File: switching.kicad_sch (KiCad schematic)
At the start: 12 parts, among them K1 SANYOU_SRD_Form_C, K2 SANYOU_SRD_Form_C, Q2 S8050_SMD, Q3 S8050_SMD

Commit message: Footprint assignment
Footprints yet to be assigned:
-U1: 74LVC125APW
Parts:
- D1, D2: footprint Diode_THT:D_DO-41_SOD81_P10.16mm_Horizontal -> Diode_SMD:D_SOD-123
- JP1, JP2, JP3, JP4: footprint (none) -> Jumper:SolderJumper-3_P2.0mm_Open_TrianglePad1.0x1.5mm
- Q2, Q3: footprint Diode_SMD:D_3220_8050Metric -> Package_TO_SOT_SMD:SOT-23
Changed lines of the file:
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@@
       (effects (font (size 1.27 1.27)) (justify left))
     )
-    (property "Footprint" "Diode_SMD:D_3220_8050Metric" (id 2) (at 208.28 120.015 0)
+    (property "Footprint" "Package_TO_SOT_SMD:SOT-23" (id 2) (at 208.28 120.015 0)
       (effects (font (size 1.27 1.27)) hide)
     )
@@
       (effects (font (size 1.27 1.27)) (justify left))
     )
-    (property "Footprint" "" (id 2) (at 87.63 107.315 0)
+    (property "Footprint" "Jumper:SolderJumper-3_P2.0mm_Open_TrianglePad1.0x1.5mm" (id 2) (at 87.63 107.315 0)
       (effects (font (size 1.27 1.27)) hide)
     )
@@
       (effects (font (size 1.27 1.27)) (justify left))
     )
-    (property "Footprint" "" (id 2) (at 110.49 80.645 0)
+    (property "Footprint" "Jumper:SolderJumper-3_P2.0mm_Open_TrianglePad1.0x1.5mm" (id 2) (at 110.49 80.645 0)
       (effects (font (size 1.27 1.27)) hide)
     )
@@
       (effects (font (size 1.27 1.27)) (justify left))
     )
-    (property "Footprint" "Diode_SMD:D_3220_8050Metric" (id 2) (at 207.645 83.185 0)
+    (property "Footprint" "Package_TO_SOT_SMD:SOT-23" (id 2) (at 207.645 83.185 0)
       (effects (font (size 1.27 1.27)) hide)
     )
@@
     (property "Reference" "D2" (id 0) (at 190.1825 122.3985 0))
     (property "Value" "1N5819" (id 1) (at 190.1825 125.1736 0))
-    (property "Footprint" "Diode_THT:D_DO-41_SOD81_P10.16mm_Horizontal" (id 2) (at 190.5 132.08 0)
+    (property "Footprint" "Diode_SMD:D_SOD-123" (id 2) (at 190.5 132.08 0)
       (effects (font (size 1.27 1.27)) hide)
     )
@@
     (property "Reference" "D1" (id 0) (at 190.1825 84.2985 0))
     (property "Value" "1N5819" (id 1) (at 190.1825 87.0736 0))
-    (property "Footprint" "Diode_THT:D_DO-41_SOD81_P10.16mm_Horizontal" (id 2) (at 190.5 93.98 0)
+    (property "Footprint" "Diode_SMD:D_SOD-123" (id 2) (at 190.5 93.98 0)
       (effects (font (size 1.27 1.27)) hide)
     )
@@
       (effects (font (size 1.27 1.27)) (justify left))
     )
-    (property "Footprint" "" (id 2) (at 110.49 107.315 0)
+    (property "Footprint" "Jumper:SolderJumper-3_P2.0mm_Open_TrianglePad1.0x1.5mm" (id 2) (at 110.49 107.315 0)
       (effects (font (size 1.27 1.27)) hide)
     )
@@
       (effects (font (size 1.27 1.27)) (justify left))
     )
-    (property "Footprint" "" (id 2) (at 87.63 80.645 0)
+    (property "Footprint" "Jumper:SolderJumper-3_P2.0mm_Open_TrianglePad1.0x1.5mm" (id 2) (at 87.63 80.645 0)
       (effects (font (size 1.27 1.27)) hide)
     )

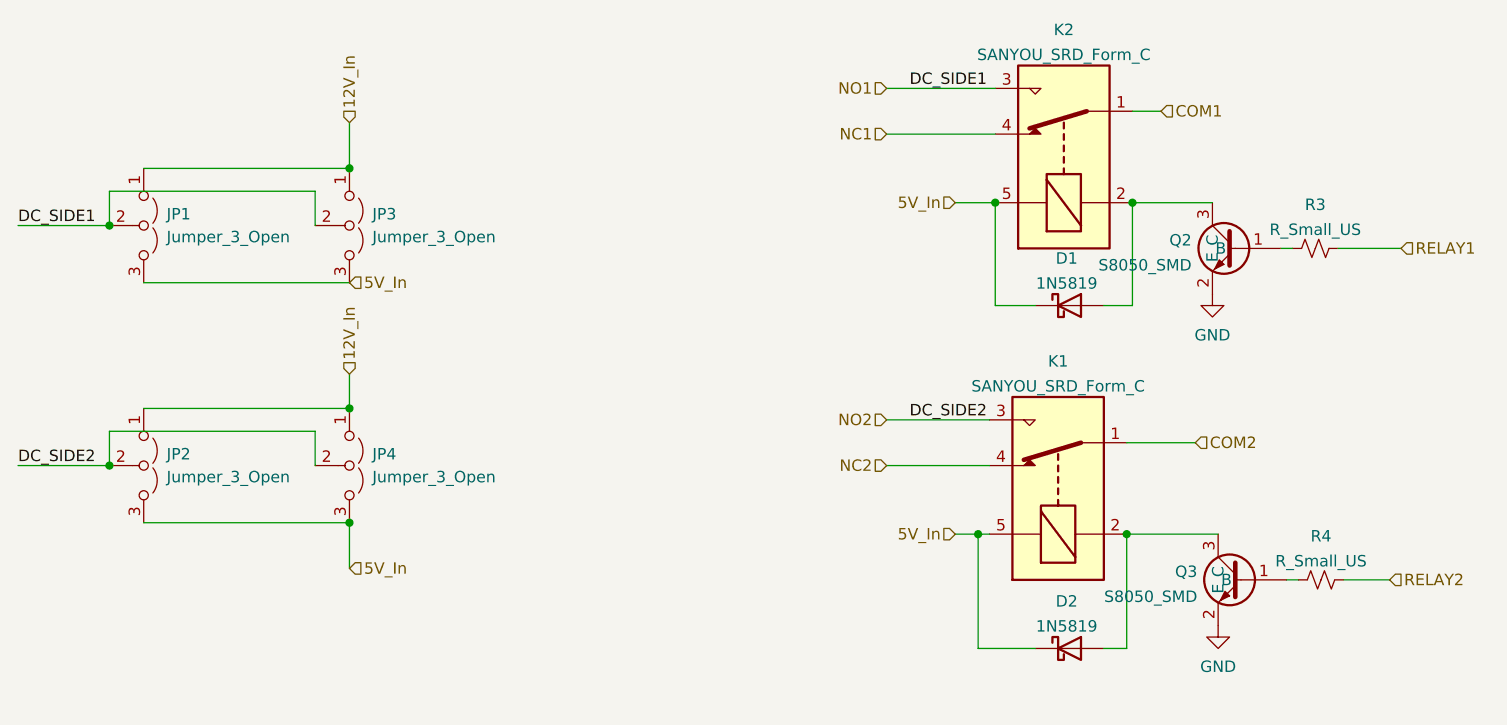
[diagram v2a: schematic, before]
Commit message: placement refinement and indicator LEDs for relays
-Crude wiring
-Fixed values
-Indicator LEDs for  relays
-Added test points
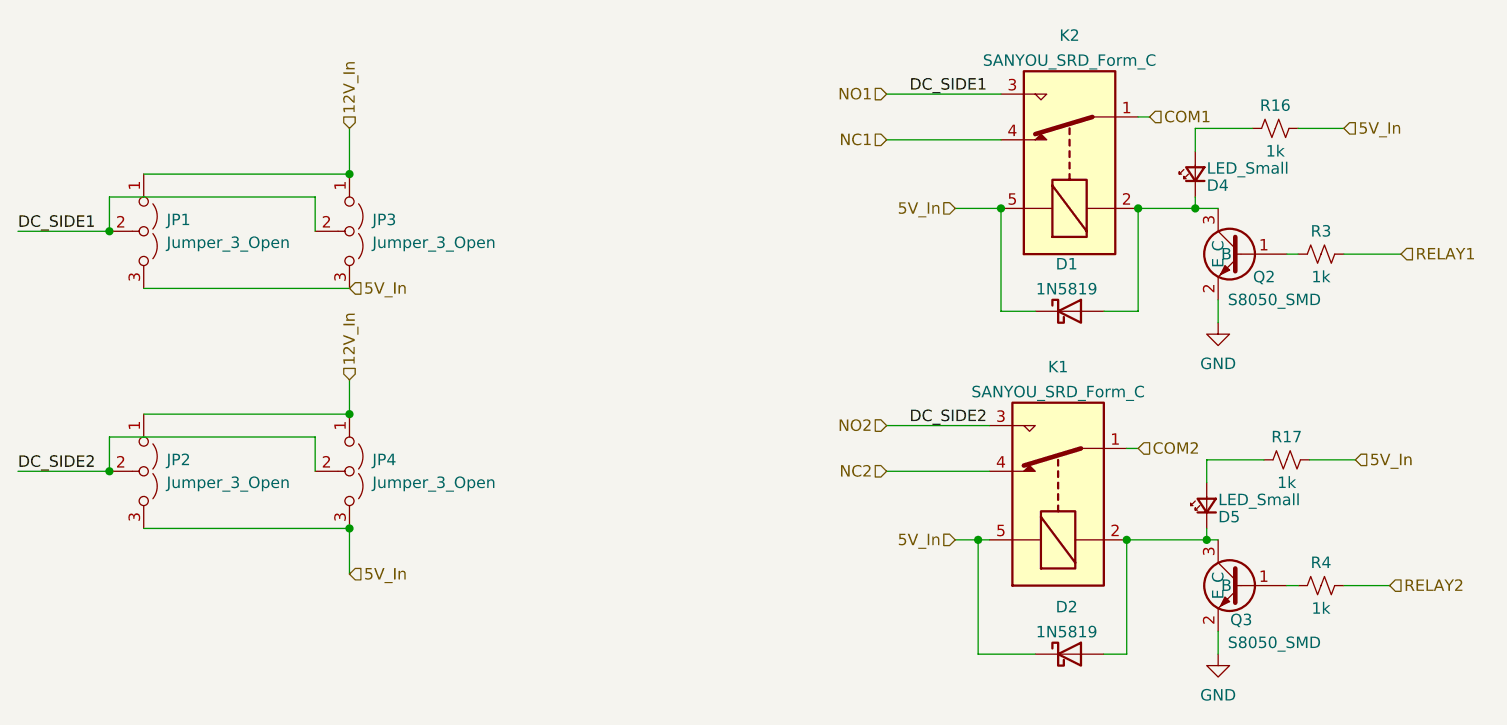
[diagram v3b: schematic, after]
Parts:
- added D4, D5: LED_Small, Diode_SMD:D_0603_1608Metric, symbol Device:LED_Small
- added R16, R17: 1k, Resistor_SMD:R_0402_1005Metric, symbol Device:R_Small_US
- R3, R4: value R_Small_US -> 1k
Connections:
- net 5V_In: now also R16.2, R17.2
- net at D1.2 (A), K2.2, Q2.3 (C): now also D4.1 (K)
- net at D2.2 (A), K1.2, Q3.3 (C): now also D5.1 (K)
- new net: D5.2 (A), R17.1
- new net: D4.2 (A), R16.1
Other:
- moved on the sheet: D1, D2, JP1, JP2, JP3, JP4, K1, K2, Q2, Q3, R3, R4

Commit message: Review and fixes on schematic and pcb.
-Updated Relay LED values.
-Fixed !RDY and R1 pin conflict on GPIO26.
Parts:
- D4, D5: value LED_Small -> Blue_LED
- R16, R17: value 1k -> 120R
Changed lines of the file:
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@@
       (effects (font (size 1.27 1.27)) (justify right))
     )
-    (property "Value" "LED_Small" (id 1) (at 207.01 111.125 90)
+    (property "Value" "Blue_LED" (id 1) (at 207.01 111.125 90)
       (effects (font (size 1.27 1.27)) (justify right))
     )
@@
     (in_bom yes) (on_board yes)
     (property "Reference" "R16" (id 0) (at 213.36 67.31 90))
-    (property "Value" "1k" (id 1) (at 213.36 72.39 90))
+    (property "Value" "120R" (id 1) (at 213.36 72.39 90))
     (property "Footprint" "Resistor_SMD:R_0402_1005Metric" (id 2) (at 213.36 69.85 0)
       (effects (font (size 1.27 1.27)) hide)
@@
       (effects (font (size 1.27 1.27)) (justify right))
     )
-    (property "Value" "LED_Small" (id 1) (at 205.74 74.295 90)
+    (property "Value" "Blue_LED" (id 1) (at 205.74 74.295 90)
       (effects (font (size 1.27 1.27)) (justify right))
     )
@@
     (in_bom yes) (on_board yes)
     (property "Reference" "R17" (id 0) (at 214.63 104.14 90))
-    (property "Value" "1k" (id 1) (at 214.63 109.22 90))
+    (property "Value" "120R" (id 1) (at 214.63 109.22 90))
     (property "Footprint" "Resistor_SMD:R_0402_1005Metric" (id 2) (at 214.63 106.68 0)
       (effects (font (size 1.27 1.27)) hide)

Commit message: Improvements made to the info in the schematic excel sheet and made the files necessary for production
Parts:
- D1, D2: Extended (none) -> 0; LCSC (none) -> C8598; Populate (none) -> 1; Price (none) -> 0.03
- D4, D5: Extended (none) -> 0; LCSC (none) -> C2286; Populate (none) -> 1; Price (none) -> 0.005
- JP1, JP2, JP3, JP4: Populate (none) -> 0
- K1, K2: Extended (none) -> 1; LCSC (none) -> C35449; Populate (none) -> 1
- Q2, Q3: Extended (none) -> 0; LCSC (none) -> C2150; Populate (none) -> 1
- R16, R17: Extended (none) -> 0; LCSC (none) -> C25079; Populate (none) -> 1
- R3, R4: Extended (none) -> 0; LCSC (none) -> C11702; Populate (none) -> 1
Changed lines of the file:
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@@
+      (effects (font (size 1.27 1.27)) hide)
+    )
+    (property "Populate" "1" (id 4) (at 190.5 73.66 0)
+      (effects (font (size 1.27 1.27)) hide)
+    )
+    (property "Extended" "1" (id 5) (at 190.5 73.66 0)
+      (effects (font (size 1.27 1.27)) hide)
+    )
+    (property "LCSC" "C35449" (id 6) (at 190.5 73.66 0)
       (effects (font (size 1.27 1.27)) hide)
     )
@@
       (effects (font (size 1.27 1.27)) hide)
     )
+    (property "Populate" "1" (id 4) (at 208.28 120.65 0)
+      (effects (font (size 1.27 1.27)) hide)
+    )
+    (property "Extended" "0" (id 5) (at 208.28 120.65 0)
+      (effects (font (size 1.27 1.27)) hide)
+    )
+    (property "LCSC" "C2150" (id 6) (at 208.28 120.65 0)
+      (effects (font (size 1.27 1.27)) hide)
+    )
     (pin "1")
     (pin "2")
@@
     )
     (property "Datasheet" "~" (id 3) (at 87.63 107.95 0)
+      (effects (font (size 1.27 1.27)) hide)
+    )
+    (property "Populate" "0" (id 4) (at 87.63 107.95 0)
       (effects (font (size 1.27 1.27)) hide)
     )
@@
     )
     (property "Datasheet" "~" (id 3) (at 205.74 111.76 90)
+      (effects (font (size 1.27 1.27)) hide)
+    )
+    (property "Extended" "0" (id 4) (at 205.74 111.76 0)
+      (effects (font (size 1.27 1.27)) hide)
+    )
+    (property "LCSC" "C2286" (id 5) (at 205.74 111.76 0)
+      (effects (font (size 1.27 1.27)) hide)
+    )
+    (property "Populate" "1" (id 6) (at 205.74 111.76 0)
+      (effects (font (size 1.27 1.27)) hide)
+    )
+    (property "Price" "0.005" (id 7) (at 205.74 111.76 0)
       (effects (font (size 1.27 1.27)) hide)
     )
@@
       (effects (font (size 1.27 1.27)) hide)
     )
+    (property "Populate" "1" (id 4) (at 213.36 69.85 0)
+      (effects (font (size 1.27 1.27)) hide)
+    )
+    (property "Extended" "0" (id 5) (at 213.36 69.85 0)
+      (effects (font (size 1.27 1.27)) hide)
+    )
+    (property "LCSC" "C25079" (id 6) (at 213.36 69.85 0)
+      (effects (font (size 1.27 1.27)) hide)
+    )
     (pin "1")
     (pin "2")
@@
       (effects (font (size 1.27 1.27)) hide)
     )
+    (property "Populate" "0" (id 4) (at 110.49 81.28 0)
+      (effects (font (size 1.27 1.27)) hide)
+    )
     (pin "1")
     (pin "2")
@@
     )
     (property "Datasheet" "" (id 3) (at 208.28 83.82 0)
+      (effects (font (size 1.27 1.27)) hide)
+    )
+    (property "Populate" "1" (id 4) (at 208.28 83.82 0)
+      (effects (font (size 1.27 1.27)) hide)
+    )
+    (property "Extended" "0" (id 5) (at 208.28 83.82 0)
+      (effects (font (size 1.27 1.27)) hide)
+    )
+    (property "LCSC" "C2150" (id 6) (at 208.28 83.82 0)
       (effects (font (size 1.27 1.27)) hide)
     )
@@
     )
     (property "Datasheet" "~" (id 3) (at 204.47 74.93 90)
+      (effects (font (size 1.27 1.27)) hide)
+    )
+    (property "Extended" "0" (id 4) (at 204.47 74.93 0)
+      (effects (font (size 1.27 1.27)) hide)
+    )
+    (property "LCSC" "C2286" (id 5) (at 204.47 74.93 0)
+      (effects (font (size 1.27 1.27)) hide)
+    )
+    (property "Populate" "1" (id 6) (at 204.47 74.93 0)
+      (effects (font (size 1.27 1.27)) hide)
+    )
+    (property "Price" "0.005" (id 7) (at 204.47 74.93 0)
       (effects (font (size 1.27 1.27)) hide)
     )
@@
       (effects (font (size 1.27 1.27)) hide)
     )
+    (property "Extended" "0" (id 4) (at 190.5 128.27 0)
+      (effects (font (size 1.27 1.27)) hide)
+    )
+    (property "LCSC" "C8598" (id 5) (at 190.5 128.27 0)
+      (effects (font (size 1.27 1.27)) hide)
+    )
+    (property "Populate" "1" (id 6) (at 190.5 128.27 0)
+      (effects (font (size 1.27 1.27)) hide)
+    )
+    (property "Price" "0.03" (id 7) (at 190.5 128.27 0)
+      (effects (font (size 1.27 1.27)) hide)
+    )
     (pin "1")
     (pin "2")
@@
       (effects (font (size 1.27 1.27)) hide)
     )
+    (property "Populate" "1" (id 4) (at 214.63 106.68 0)
+      (effects (font (size 1.27 1.27)) hide)
+    )
+    (property "Extended" "0" (id 5) (at 214.63 106.68 0)
+      (effects (font (size 1.27 1.27)) hide)
+    )
+    (property "LCSC" "C25079" (id 6) (at 214.63 106.68 0)
+      (effects (font (size 1.27 1.27)) hide)
+    )
     (pin "1")
     (pin "2")
@@
       (effects (font (size 1.27 1.27)) hide)
     )
+    (property "Extended" "0" (id 4) (at 190.5 90.17 0)
+      (effects (font (size 1.27 1.27)) hide)
+    )
+    (property "LCSC" "C8598" (id 5) (at 190.5 90.17 0)
+      (effects (font (size 1.27 1.27)) hide)
+    )
+    (property "Populate" "1" (id 6) (at 190.5 90.17 0)
+      (effects (font (size 1.27 1.27)) hide)
+    )
+    (property "Price" "0.03" (id 7) (at 190.5 90.17 0)
+      (effects (font (size 1.27 1.27)) hide)
+    )
     (pin "1")
     (pin "2")
@@
       (effects (font (size 1.27 1.27)) hide)
     )
+    (property "Populate" "1" (id 4) (at 218.44 120.65 0)
+      (effects (font (size 1.27 1.27)) hide)
+    )
+    (property "Extended" "0" (id 5) (at 218.44 120.65 0)
+      (effects (font (size 1.27 1.27)) hide)
+    )
+    (property "LCSC" "C11702" (id 6) (at 218.44 120.65 0)
+      (effects (font (size 1.27 1.27)) hide)
+    )
     (pin "1")
     (pin "2")
@@
     )
     (property "Datasheet" "~" (id 3) (at 110.49 107.95 0)
+      (effects (font (size 1.27 1.27)) hide)
+    )
+    (property "Populate" "0" (id 4) (at 110.49 107.95 0)
       (effects (font (size 1.27 1.27)) hide)
     )
@@
       (effects (font (size 1.27 1.27)) hide)
     )
+    (property "Populate" "1" (id 4) (at 189.23 110.49 0)
+      (effects (font (size 1.27 1.27)) hide)
+    )
+    (property "Extended" "1" (id 5) (at 189.23 110.49 0)
+      (effects (font (size 1.27 1.27)) hide)
+    )
+    (property "LCSC" "C35449" (id 6) (at 189.23 110.49 0)
+      (effects (font (size 1.27 1.27)) hide)
+    )
     (pin "1")
     (pin "2")
@@
       (effects (font (size 1.27 1.27)) hide)
     )
+    (property "Populate" "1" (id 4) (at 218.44 83.82 0)
+      (effects (font (size 1.27 1.27)) hide)
+    )
+    (property "Extended" "0" (id 5) (at 218.44 83.82 0)
+      (effects (font (size 1.27 1.27)) hide)
+    )
+    (property "LCSC" "C11702" (id 6) (at 218.44 83.82 0)
+      (effects (font (size 1.27 1.27)) hide)
+    )
     (pin "1")
     (pin "2")
@@
       (effects (font (size 1.27 1.27)) hide)
     )
+    (property "Populate" "0" (id 4) (at 87.63 81.28 0)
+      (effects (font (size 1.27 1.27)) hide)
+    )

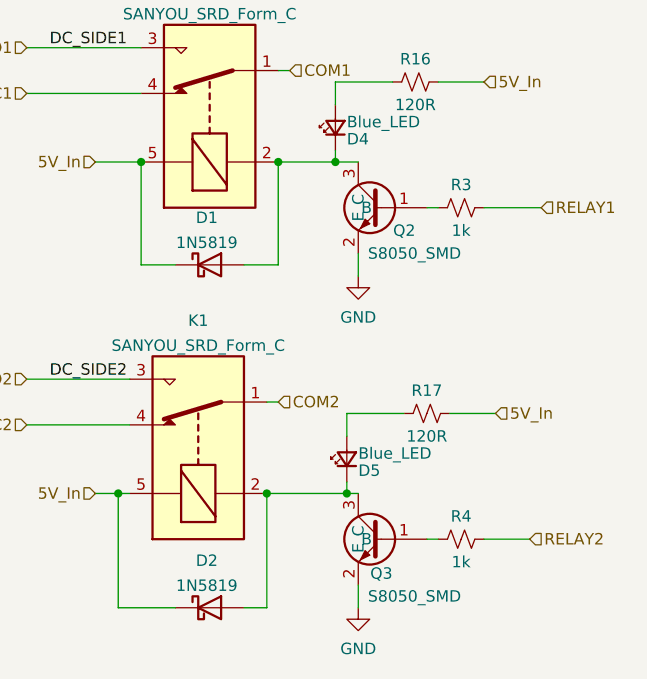
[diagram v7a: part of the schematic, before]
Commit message: Changes made to the AD7730 circuit. HX711 circuit added and AD7730 sidestepped.
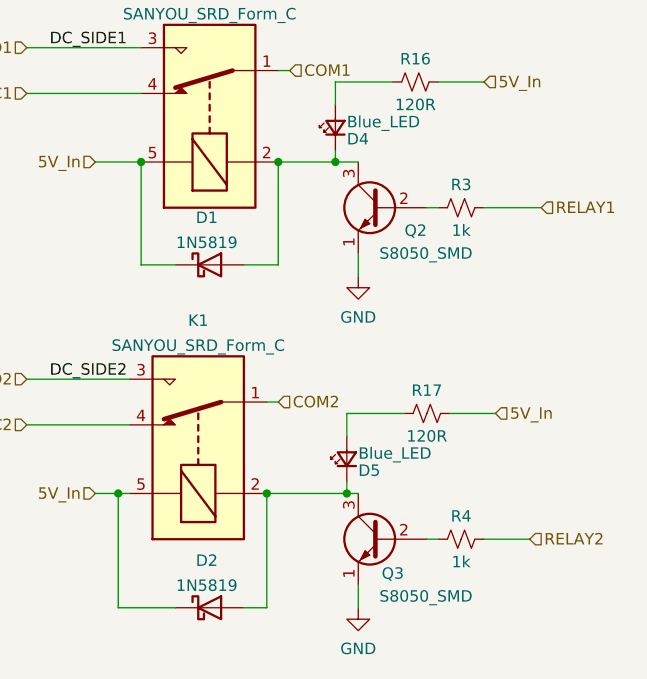
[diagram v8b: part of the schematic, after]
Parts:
- Q2, Q3: footprint Package_TO_SOT_SMD:SOT-23 -> Package_TO_SOT_THT:TO-92_Inline; symbol MyDevices:S8050_SMD -> Transistor_BJT:S8050
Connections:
- net GND: now also Q2.1 (E), Q3.1 (E); no longer Q2.2 (E), Q3.2 (E)
- net at R4.1: now also Q3.2 (B); no longer Q3.1 (B)
- net at R3.1: now also Q2.2 (B); no longer Q2.1 (B)
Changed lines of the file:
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@@
     )
   )
-  (symbol (lib_id "MyDevices:S8050_SMD") (at 208.28 120.65 0) (mirror y) (unit 1)
+  (symbol (lib_id "Transistor_BJT:S8050") (at 209.55 120.65 0) (mirror y) (unit 1)
     (in_bom yes) (on_board yes) (dnp no)
-    (property "Reference" "Q3" (at 210.82 124.46 0)
+    (property "Reference" "Q3" (at 212.09 124.46 0)
       (effects (font (size 1.27 1.27)) (justify left))
     )
-    (property "Value" "S8050_SMD" (at 218.44 127 0)
+    (property "Value" "S8050_SMD" (at 219.71 127 0)
       (effects (font (size 1.27 1.27)) (justify left))
     )
-    (property "Footprint" "Package_TO_SOT_SMD:SOT-23" (at 208.28 120.65 0)
+    (property "Footprint" "Package_TO_SOT_THT:TO-92_Inline" (at 204.47 122.555 0)
+      (effects (font (size 1.27 1.27) italic) (justify left) hide)
+    )
+    (property "Datasheet" "http://www.unisonic.com.tw/datasheet/S8050.pdf" (at 209.55 120.65 0)
+      (effects (font (size 1.27 1.27)) (justify left) hide)
+    )
+    (property "Populate" "1" (at 209.55 120.65 0)
       (effects (font (size 1.27 1.27)) hide)
     )
-    (property "Datasheet" "" (at 208.28 120.65 0)
+    (property "Extended" "0" (at 209.55 120.65 0)
       (effects (font (size 1.27 1.27)) hide)
     )
-    (property "Populate" "1" (at 208.28 120.65 0)
-      (effects (font (size 1.27 1.27)) hide)
-    )
-    (property "Extended" "0" (at 208.28 120.65 0)
-      (effects (font (size 1.27 1.27)) hide)
-    )
-    (property "LCSC" "C2150" (at 208.28 120.65 0)
+    (property "LCSC" "C2150" (at 209.55 120.65 0)
       (effects (font (size 1.27 1.27)) hide)
     )
@@
     )
   )
-  (symbol (lib_id "MyDevices:S8050_SMD") (at 208.28 83.82 0) (mirror y) (unit 1)
+  (symbol (lib_id "Transistor_BJT:S8050") (at 209.55 83.82 0) (mirror y) (unit 1)
     (in_bom yes) (on_board yes) (dnp no)
-    (property "Reference" "Q2" (at 213.36 86.36 0)
+    (property "Reference" "Q2" (at 214.63 86.36 0)
       (effects (font (size 1.27 1.27)) (justify left))
     )
-    (property "Value" "S8050_SMD" (at 218.44 88.9 0)
+    (property "Value" "S8050_SMD" (at 219.71 88.9 0)
       (effects (font (size 1.27 1.27)) (justify left))
     )
-    (property "Footprint" "Package_TO_SOT_SMD:SOT-23" (at 208.28 83.82 0)
+    (property "Footprint" "Package_TO_SOT_THT:TO-92_Inline" (at 204.47 85.725 0)
+      (effects (font (size 1.27 1.27) italic) (justify left) hide)
+    )
+    (property "Datasheet" "http://www.unisonic.com.tw/datasheet/S8050.pdf" (at 209.55 83.82 0)
+      (effects (font (size 1.27 1.27)) (justify left) hide)
+    )
+    (property "Populate" "1" (at 209.55 83.82 0)
       (effects (font (size 1.27 1.27)) hide)
     )
-    (property "Datasheet" "" (at 208.28 83.82 0)
+    (property "Extended" "0" (at 209.55 83.82 0)
       (effects (font (size 1.27 1.27)) hide)
     )
-    (property "Populate" "1" (at 208.28 83.82 0)
+    (property "LCSC" "C2150" (at 209.55 83.82 0)
       (effects (font (size 1.27 1.27)) hide)
     )
-    (property "Extended" "0" (at 208.28 83.82 0)
-      (effects (font (size 1.27 1.27)) hide)
-    )
-    (property "LCSC" "C2150" (at 208.28 83.82 0)
-      (effects (font (size 1.27 1.27)) hide)
-    )
